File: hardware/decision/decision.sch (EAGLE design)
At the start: 8 parts, among them IC1 7805T, IC2 A1301UA

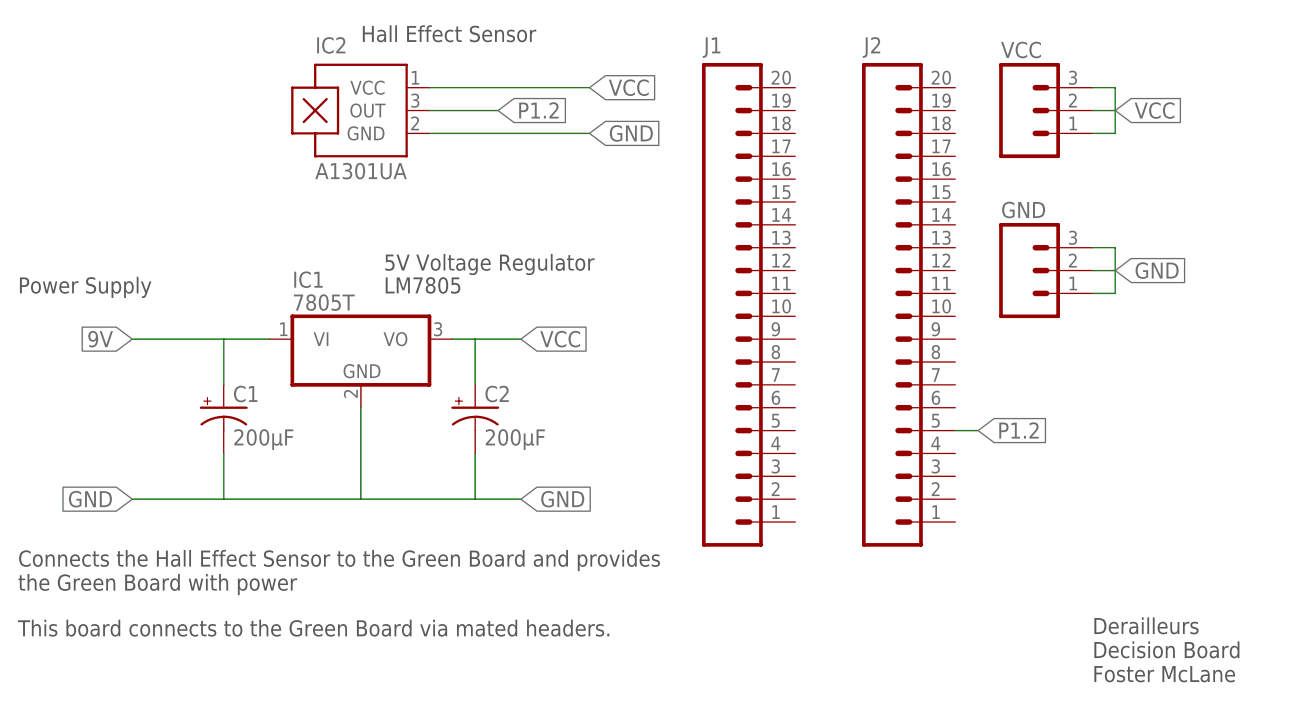
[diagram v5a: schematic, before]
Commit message: Finish routing all boards, schematics are consitant, and all deliverable requirements are met..
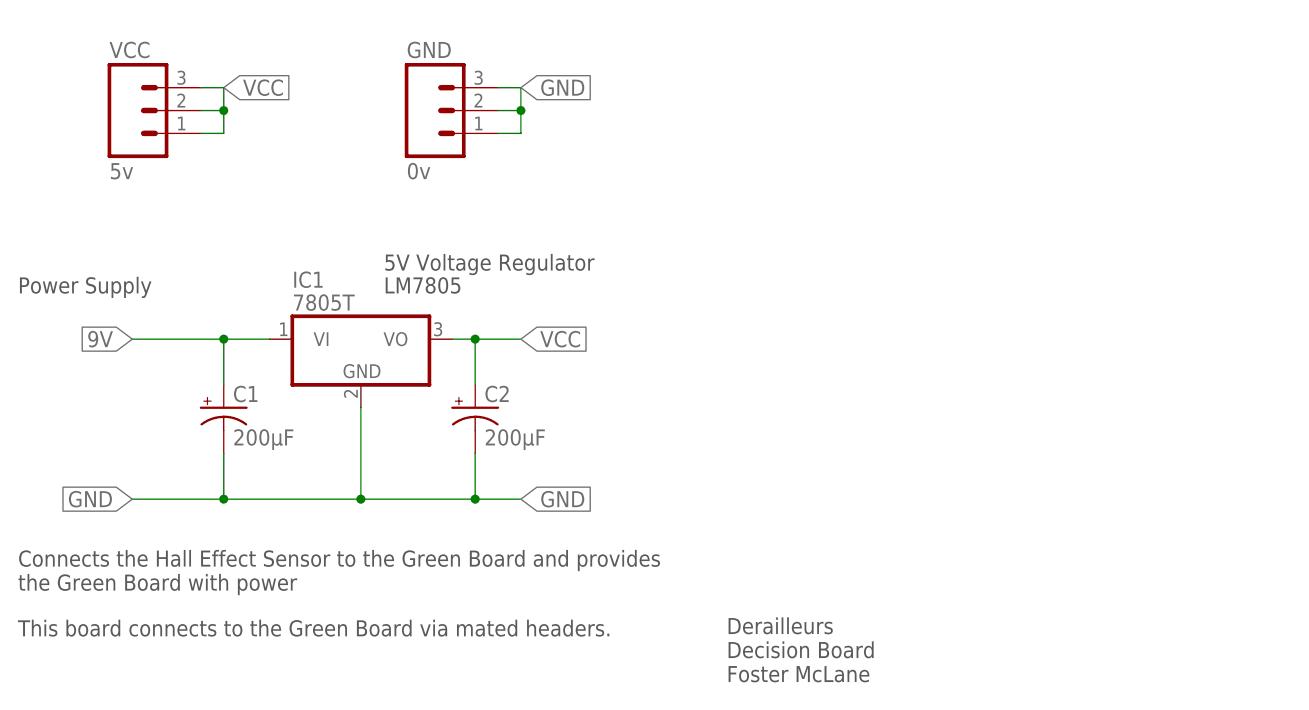
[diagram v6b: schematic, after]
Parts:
- removed IC2: A1301UA, allegro:A1301UA
- removed J1, J2: (no value), SparkFun-Connectors:M20
- GND: value (none) -> 0v; device SparkFun-Connectors:M03LOCK -> SparkFun-Connectors:M03PTH
- VCC: value (none) -> 5v; device SparkFun-Connectors:M03LOCK -> SparkFun-Connectors:M03PTH
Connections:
- removed net P1.2: IC2.OUT, J2.5
- net GND: no longer IC2.GND
- net VCC: no longer IC2.VCC
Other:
- note removed: "Hall Effect Sensor"
- moved on the sheet: GND, VCC
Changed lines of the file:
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@@
 <parts>
 <part name="IC1" library="linear" deviceset="78*" device="T" technology="05"/>
-<part name="IC2" library="allegro" deviceset="A13*?" device="UA" technology="01"/>
 <part name="C1" library="SparkFun-Capacitors" deviceset="CAP_POL" device="PTH1" value="200µF"/>
 <part name="C2" library="SparkFun-Capacitors" deviceset="CAP_POL" device="PTH1" value="200µF"/>
-<part name="J1" library="SparkFun-Connectors" deviceset="M20" device=""/>
-<part name="J2" library="SparkFun-Connectors" deviceset="M20" device=""/>
-<part name="VCC" library="SparkFun-Connectors" deviceset="M03" device="LOCK"/>
-<part name="GND" library="SparkFun-Connectors" deviceset="M03" device="LOCK"/>
+<part name="VCC" library="SparkFun-Connectors" deviceset="M03" device="PTH" value="5v"/>
+<part name="GND" library="SparkFun-Connectors" deviceset="M03" device="PTH" value="0v"/>
 </parts>
 <sheets>
@@
 <plain>
 <text x="45.72" y="27.94" size="1.778" layer="97">LM7805</text>
-<text x="43.18" y="55.88" size="1.778" layer="97">Hall Effect Sensor</text>
 <text x="45.72" y="30.48" size="1.778" layer="97">5V Voltage Regulator</text>
 <text x="5.08" y="-5.08" size="1.778" layer="97">Connects the Hall Effect Sensor to the Green Board and provides
 the Green Board with power</text>
 <text x="5.08" y="-10.16" size="1.778" layer="97">This board connects to the Green Board via mated headers.</text>
-<text x="124.46" y="-15.24" size="1.778" layer="97">Derailleurs
+<text x="83.82" y="-15.24" size="1.778" layer="97">Derailleurs
 Decision Board
 Foster McLane</text>
 <text x="5.08" y="27.94" size="1.778" layer="97">Power Supply</text>
-<frame x1="-12.7" y1="-22.86" x2="149.86" y2="68.58" columns="8" rows="5" layer="91"/>
+<frame x1="-12.7" y1="-22.86" x2="114.3" y2="68.58" columns="8" rows="5" layer="91"/>
 </plain>
 <instances>
 <instance part="IC1" gate="A1" x="43.18" y="22.86"/>
-<instance part="IC2" gate="G$1" x="43.18" y="48.26"/>
 <instance part="C1" gate="G$1" x="27.94" y="15.24"/>
 <instance part="C2" gate="G$1" x="55.88" y="15.24"/>
-<instance part="J1" gate="G$1" x="81.28" y="-2.54"/>
-<instance part="J2" gate="G$1" x="99.06" y="-2.54"/>
-<instance part="VCC" gate="J$1" x="116.84" y="48.26"/>
-<instance part="GND" gate="J$1" x="116.84" y="30.48"/>
+<instance part="VCC" gate="J$1" x="17.78" y="48.26"/>
+<instance part="GND" gate="J$1" x="50.8" y="48.26"/>
 </instances>
 <busses>
@@
 <segment>
 <pinref part="IC1" gate="A1" pin="VI"/>
+<label x="17.78" y="22.86" size="1.778" layer="95" rot="R180" xref="yes"/>
 <wire x1="17.78" y1="22.86" x2="27.94" y2="22.86" width="0.1524" layer="91"/>
+<junction x="27.94" y="22.86"/>
+<wire x1="27.94" y1="22.86" x2="33.02" y2="22.86" width="0.1524" layer="91"/>
 <pinref part="C1" gate="G$1" pin="+"/>
-<wire x1="27.94" y1="22.86" x2="33.02" y2="22.86" width="0.1524" layer="91"/>
-<wire x1="27.94" y1="17.78" x2="27.94" y2="22.86" width="0.1524" layer="91"/>
-<label x="17.78" y="22.86" size="1.778" layer="95" rot="R180" xref="yes"/>
+<wire x1="27.94" y1="22.86" x2="27.94" y2="17.78" width="0.1524" layer="91"/>
 </segment>
 </net>
@@
 <pinref part="IC1" gate="A1" pin="GND"/>
 <wire x1="43.18" y1="15.24" x2="43.18" y2="5.08" width="0.1524" layer="91"/>
-<wire x1="43.18" y1="5.08" x2="27.94" y2="5.08" width="0.1524" layer="91"/>
-<wire x1="43.18" y1="5.08" x2="55.88" y2="5.08" width="0.1524" layer="91"/>
 <label x="60.96" y="5.08" size="1.778" layer="95" xref="yes"/>
-<pinref part="C1" gate="G$1" pin="-"/>
 <wire x1="55.88" y1="5.08" x2="60.96" y2="5.08" width="0.1524" layer="91"/>
-<wire x1="27.94" y1="10.16" x2="27.94" y2="5.08" width="0.1524" layer="91"/>
 <pinref part="C2" gate="G$1" pin="-"/>
 <wire x1="55.88" y1="10.16" x2="55.88" y2="5.08" width="0.1524" layer="91"/>
+<label x="17.78" y="5.08" size="1.778" layer="95" rot="R180" xref="yes"/>
+<wire x1="43.18" y1="5.08" x2="27.94" y2="5.08" width="0.1524" layer="91"/>
+<junction x="43.18" y="5.08"/>
 <wire x1="27.94" y1="5.08" x2="17.78" y2="5.08" width="0.1524" layer="91"/>
-<label x="127" y="30.48" size="1.778" layer="95" xref="yes"/>
-<label x="17.78" y="5.08" size="1.778" layer="95" rot="R180" xref="yes"/>
-</segment>
-<segment>
-<pinref part="IC2" gate="G$1" pin="GND"/>
-<wire x1="50.8" y1="45.72" x2="68.58" y2="45.72" width="0.1524" layer="91"/>
-<label x="68.58" y="45.72" size="1.778" layer="95" xref="yes"/>
+<wire x1="55.88" y1="5.08" x2="43.18" y2="5.08" width="0.1524" layer="91"/>
+<junction x="55.88" y="5.08"/>
+<junction x="27.94" y="5.08"/>
+<pinref part="C1" gate="G$1" pin="-"/>
+<wire x1="27.94" y1="5.08" x2="27.94" y2="10.16" width="0.1524" layer="91"/>
 </segment>
 <segment>
 <pinref part="GND" gate="J$1" pin="3"/>
-<wire x1="124.46" y1="33.02" x2="127" y2="33.02" width="0.1524" layer="91"/>
-<wire x1="127" y1="33.02" x2="127" y2="30.48" width="0.1524" layer="91"/>
+<wire x1="58.42" y1="50.8" x2="60.96" y2="50.8" width="0.1524" layer="91"/>
+<label x="60.96" y="50.8" size="1.778" layer="95" xref="yes"/>
 <pinref part="GND" gate="J$1" pin="2"/>
-<wire x1="127" y1="30.48" x2="124.46" y2="30.48" width="0.1524" layer="91"/>
+<wire x1="58.42" y1="48.26" x2="60.96" y2="48.26" width="0.1524" layer="91"/>
+<wire x1="60.96" y1="48.26" x2="60.96" y2="50.8" width="0.1524" layer="91"/>
 <pinref part="GND" gate="J$1" pin="1"/>
-<wire x1="124.46" y1="27.94" x2="127" y2="27.94" width="0.1524" layer="91"/>
-<wire x1="127" y1="27.94" x2="127" y2="30.48" width="0.1524" layer="91"/>
+<wire x1="58.42" y1="45.72" x2="60.96" y2="45.72" width="0.1524" layer="91"/>
+<wire x1="60.96" y1="45.72" x2="60.96" y2="48.26" width="0.1524" layer="91"/>
+<junction x="60.96" y="48.26"/>
 </segment>
 </net>
@@
 <wire x1="55.88" y1="22.86" x2="60.96" y2="22.86" width="0.1524" layer="91"/>
 <wire x1="55.88" y1="17.78" x2="55.88" y2="22.86" width="0.1524" layer="91"/>
-<label x="127" y="48.26" size="1.778" layer="95" xref="yes"/>
+<junction x="55.88" y="22.86"/>
 </segment>
 <segment>
-<pinref part="IC2" gate="G$1" pin="VCC"/>
-<wire x1="50.8" y1="50.8" x2="68.58" y2="50.8" width="0.1524" layer="91"/>
-<label x="68.58" y="50.8" size="1.778" layer="95" xref="yes"/>
-</segment>
-<segment>
+<pinref part="VCC" gate="J$1" pin="3"/>
+<wire x1="25.4" y1="50.8" x2="27.94" y2="50.8" width="0.1524" layer="91"/>
+<label x="27.94" y="50.8" size="1.778" layer="95" xref="yes"/>
+<pinref part="VCC" gate="J$1" pin="2"/>
+<wire x1="25.4" y1="48.26" x2="27.94" y2="48.26" width="0.1524" layer="91"/>
+<wire x1="27.94" y1="48.26" x2="27.94" y2="50.8" width="0.1524" layer="91"/>
 <pinref part="VCC" gate="J$1" pin="1"/>
-<wire x1="124.46" y1="45.72" x2="127" y2="45.72" width="0.1524" layer="91"/>
-<pinref part="VCC" gate="J$1" pin="3"/>
-<wire x1="124.46" y1="50.8" x2="127" y2="50.8" width="0.1524" layer="91"/>
-<wire x1="127" y1="50.8" x2="127" y2="48.26" width="0.1524" layer="91"/>
-<pinref part="VCC" gate="J$1" pin="2"/>
-<wire x1="127" y1="48.26" x2="127" y2="45.72" width="0.1524" layer="91"/>
-<wire x1="124.46" y1="48.26" x2="127" y2="48.26" width="0.1524" layer="91"/>
+<wire x1="25.4" y1="45.72" x2="27.94" y2="45.72" width="0.1524" layer="91"/>
+<wire x1="27.94" y1="45.72" x2="27.94" y2="48.26" width="0.1524" layer="91"/>
+<junction x="27.94" y="48.26"/>
 </segment>
 </net>
-<net name="P1.2" class="0">
-<segment>
-<pinref part="IC2" gate="G$1" pin="OUT"/>
-<wire x1="50.8" y1="48.26" x2="58.42" y2="48.26" width="0.1524" layer="91"/>
-<label x="58.42" y="48.26" size="1.778" layer="95" xref="yes"/>
-</segment>
-<segment>
-<pinref part="J2" gate="G$1" pin="5"/>
-<wire x1="109.22" y1="12.7" x2="111.76" y2="12.7" width="0.1524" layer="91"/>
-<label x="111.76" y="12.7" size="1.778" layer="95" xref="yes"/>
-</segment>
-</net>
